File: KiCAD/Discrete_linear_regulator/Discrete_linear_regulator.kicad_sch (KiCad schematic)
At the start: 40 parts, among them J1 Conn_01x06, Q1 PZT2222AT3G, Q10 BC857, Q11 BC857, Q2 BC857, Q3 BC857, Q4 PZT2222AT3G, Q5 PZT2907AT3G, Q8 PZT2907AT3G, U1 LM4562

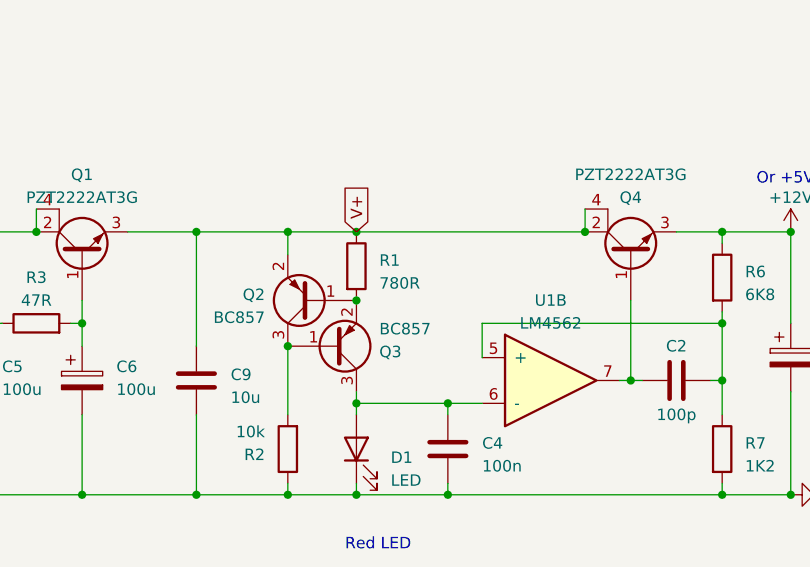
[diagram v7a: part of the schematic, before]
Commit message: Schematic update Liniar
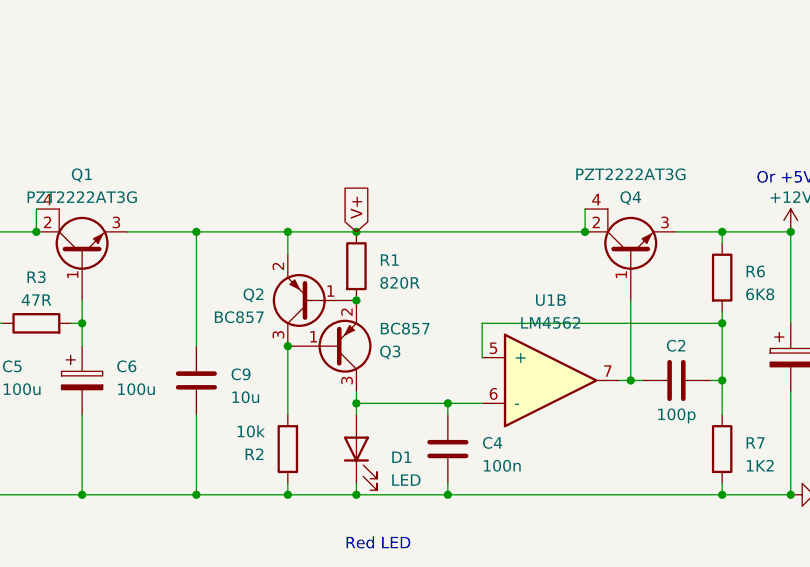
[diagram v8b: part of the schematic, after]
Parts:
- R1: value 780R -> 820R
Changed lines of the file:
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@@
       (effects (font (size 1.27 1.27)) hide)
     )
-    (property "Datasheet" "~" (at 74.93 69.85 0)
+    (property "Datasheet" "https://nl.mouser.com/ProductDetail/YAGEO/RT0402FRE0747RL?qs=sGAEpiMZZMvdGkrng054t0q%2FxTkBpeSrrs0gjydReCc%3D" (at 74.93 69.85 0)
       (effects (font (size 1.27 1.27)) hide)
     )
@@
       (effects (font (size 1.27 1.27)) hide)
     )
-    (property "Datasheet" "~" (at 102.87 83.82 0)
+    (property "Datasheet" "https://nl.mouser.com/ProductDetail/Vishay-Dale/CRCW040210K0FKEDC?qs=E3Y5ESvWgWPiNLcGzwCGPg%3D%3D" (at 102.87 83.82 0)
       (effects (font (size 1.27 1.27)) hide)
     )
@@
       (effects (font (size 1.27 1.27)) hide)
     )
-    (property "Datasheet" "~" (at 62.23 64.77 0)
+    (property "Datasheet" "https://nl.mouser.com/ProductDetail/YAGEO/RT0402FRE07100RL?qs=sGAEpiMZZMvdGkrng054t%252BKCHBXLTLydY05E6nMrbFY%3D" (at 62.23 64.77 0)
       (effects (font (size 1.27 1.27)) hide)
     )
@@
       (effects (font (size 1.27 1.27)) hide)
     )
-    (property "Datasheet" "~" (at 62.23 76.2 0)
+    (property "Datasheet" "https://nl.mouser.com/ProductDetail/Vishay-Dale/CRCW0402100KFKEDC?qs=E3Y5ESvWgWPiKlL6PvtQMQ%3D%3D" (at 62.23 76.2 0)
       (effects (font (size 1.27 1.27)) hide)
     )
@@
       (effects (font (size 1.27 1.27)) (justify left))
     )
-    (property "Value" "780R" (at 113.03 65.405 0)
+    (property "Value" "820R" (at 113.03 65.405 0)
       (effects (font (size 1.27 1.27)) (justify left))
     )
@@
       (effects (font (size 1.27 1.27)) hide)
     )
-    (property "Datasheet" "~" (at 110.49 63.5 0)
-      (effects (font (size 1.27 1.27)) hide)
-    )
+    (property "Datasheet" "https://nl.mouser.com/ProductDetail/YAGEO/RT0402FRE07820RL?qs=iFuT%252BolKbR7tOecAWZmkmw%3D%3D" (at 110.49 63.5 0)
+      (effects (font (size 1.27 1.27)) hide)
+    )
